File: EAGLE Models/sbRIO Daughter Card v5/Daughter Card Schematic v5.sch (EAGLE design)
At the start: 110 parts, among them Q1 MMBT4403-7-F, Q10 MMBT4403-7-F, Q11 MMBT4401-7-F, Q13 MMBT4401-7-F, Q14 MMBT4403-7-F, Q15 MMBT4403-7-F, Q16 MMBT4403-7-F, Q17 MMBT4403-7-F, Q2 MMBT4403-7-F, Q3 MMBT4403-7-F, Q4 MMBT4403-7-F, Q5 MMBT4403-7-F, Q6 MMBT4403-7-F, Q7 MMBT4403-7-F, Q8 MMBT4403-7-F, Q9 MMBT4401-7-F, U1 MMBT4403-7-F, U2 ADXL345, U3 L3G4200D

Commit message: made many changes
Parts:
- removed DASHBOARD_CONN, HV_BOX_CONN, PEDAL_CONN, SHOCK_POT_CONN, WHEEL_SPEED: EN3_PCB_8, formula electric:EN3_PCB_8
- removed Q14, Q15, Q16, Q17: MMBT4403-7-F, formula electric:MMBT4403-7-F
- removed R26, R28, R30, R32: 10k, resistor:R-US_R0402
- removed R27, R29, R31, R33: 1k, resistor:R-US_R0402
- added ACCUMULATOR_CONN: RJ45-6L21-S, con-tycoelectronics:RJ45-6L21-S
- added AIO_PO_CONN, TUB_CONN: 2516-5, con-3m:2516-5
- added F19, F20, F21, F22, F23, F24, F25, F26: (no value), resistor:R-EU_R0402
- added Q12, Q18, Q19, Q20: MMBT4403-7-F, formula electric:MMBT4403-7-F
- added R37, R38, R39, R40, R41, R42, R43, R44: 4.7k, resistor:R-US_R0402
- added U$1, U$4, U$5, U$6: MMBT4401-7-F, formula electric:MMBT4401-7-F
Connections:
- removed net N$84: Q17.B, R32.2
- new net DIO25: R41.1
- new net DIO26: R37.2
- new net DIO27: R38.2
- new net DIO28: R39.2
- new net N$29: AIO_PO_CONN-3.KL, F19.2
- new net N$30: Q19.B, R40.2
- new net N$31: R40.1, U$1.C
- new net N$32: R41.2, U$1.B
- new net N$85: Q12.B, R42.2
- new net N$86: R42.1, U$4.C
- new net N$87: R37.1, U$4.B
- new net N$88: Q18.B, R43.2
- new net N$89: R43.1, U$5.C
- new net N$90: R38.1, U$5.B
- new net N$91: Q20.B, R44.2
- new net N$92: R44.1, U$6.C
- new net N$93: R39.1, U$6.B
- new net PO1: F26.1, Q19.C
- new net PO2: F25.1, Q12.C
- new net PO3: F24.1, Q18.C
- new net PO4: F23.1, Q20.C
- net 12V: now also F19.1, Q12.E, Q18.E, Q19.E, Q20.E; no longer F15.2
- net 3.3V: no longer Q14.E, Q15.E, Q16.E, Q17.E
- net AI1: now also ACCUMULATOR_CONN.5; no longer HV_BOX_CONN.P$5
- net AI10: now also AIO_PO_CONN-5.KL; no longer SHOCK_POT_CONN.P$2
- net AI11: now also AIO_PO_CONN-4.KL; no longer SHOCK_POT_CONN.P$3
- net AI15: now also AIO_PO_CONN-8.KL
- net AI2: now also ACCUMULATOR_CONN.6; no longer HV_BOX_CONN.P$6
- net AI3: now also TUB_CONN-10.KL; no longer PEDAL_CONN.P$7
- net AI4: now also TUB_CONN-9.KL; no longer PEDAL_CONN.P$8
- net AI7: now also TUB_CONN-13.KL; no longer PEDAL_CONN.P$4
- net AI8: now also AIO_PO_CONN-7.KL; no longer SHOCK_POT_CONN.P$8
- net AI9: now also AIO_PO_CONN-6.KL; no longer SHOCK_POT_CONN.P$1
- net AO0: now also F22.1
- net AO1: now also F21.1
- net AO2: now also F20.1
- net AO3: now also F15.1
- net CAN_GND: now also ACCUMULATOR_CONN.1, ACCUMULATOR_CONN.S@1, ACCUMULATOR_CONN.S@2, ACCUMULATOR_CONN.S@3, ACCUMULATOR_CONN.S@4; no longer HV_BOX_CONN.P$1
- net CAN_H: now also ACCUMULATOR_CONN.3, TUB_CONN-7.KL; no longer DASHBOARD_CONN.P$2, HV_BOX_CONN.P$3
- net CAN_L: now also ACCUMULATOR_CONN.4, TUB_CONN-6.KL; no longer DASHBOARD_CONN.P$3, HV_BOX_CONN.P$4
- net DI09: now also TUB_CONN-8.KL; no longer DASHBOARD_CONN.P$1
- net DIO0: no longer Q14.C, R27.2
- net DIO1: no longer Q17.C, R33.2
- net DIO2: no longer Q16.C, R31.2
- net DIO3: no longer Q15.C, R29.2
- net GND: now also AIO_PO_CONN-1.KL, TUB_CONN-11.KL, U$1.E, U$4.E, U$5.E, U$6.E; no longer R27.1, R29.1, R31.1, R33.1, SHOCK_POT_CONN.P$7, WHEEL_SPEED.P$5
- net N$10: now also AIO_PO_CONN-12.KL, F22.2; no longer R26.1, WHEEL_SPEED.P$8
- net N$13: now also ACCUMULATOR_CONN.7; no longer HV_BOX_CONN.P$7
- net N$14: now also ACCUMULATOR_CONN.8; no longer HV_BOX_CONN.P$8
- net N$20: now also AIO_PO_CONN-2.KL; no longer SHOCK_POT_CONN.P$4
- net N$21: now also AIO_PO_CONN-13.KL, F23.2; no longer F15.1, WHEEL_SPEED.P$4
- net N$22: now also TUB_CONN-12.KL; no longer PEDAL_CONN.P$5
- net N$23: now also TUB_CONN-5.KL; no longer DASHBOARD_CONN.P$4
- net N$24: now also TUB_CONN-4.KL; no longer DASHBOARD_CONN.P$5
- net N$3: now also AIO_PO_CONN-9.KL, F15.2; no longer R32.1, WHEEL_SPEED.P$1
- net N$33: now also TUB_CONN-3.KL; no longer DASHBOARD_CONN.P$6
- net N$34: now also TUB_CONN-2.KL; no longer DASHBOARD_CONN.P$7
- net N$35: now also TUB_CONN-1.KL; no longer DASHBOARD_CONN.P$8
- net N$6: now also AIO_PO_CONN-10.KL, F20.2; no longer Q16.B, R30.2
- net N$81: now also AIO_PO_CONN-14.KL, F24.2; no longer Q14.B, R26.2
- net N$82: now also AIO_PO_CONN-15.KL, F25.2; no longer Q15.B, R28.2
- net N$83: now also AIO_PO_CONN-16.KL, F26.2; no longer R30.1, WHEEL_SPEED.P$2
- net N$9: now also AIO_PO_CONN-11.KL, F21.2; no longer R28.1, WHEEL_SPEED.P$3
- net SHIELD: now also ACCUMULATOR_CONN.2; no longer HV_BOX_CONN.P$2
- net STEERING_POS: now also TUB_CONN-14.KL; no longer PEDAL_CONN.P$3
- net THROTTLE_1: now also TUB_CONN-16.KL; no longer PEDAL_CONN.P$1
- net THROTTLE_2: now also TUB_CONN-15.KL; no longer PEDAL_CONN.P$2
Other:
- note added: "need fusing"
- moved on the sheet: D5, D6, F10, F11, F12, F13, F14, F15, F16, F7, F8, F9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

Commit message: Changed daughter card stuff
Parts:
- removed Q12, Q18, Q19, Q20: MMBT4403-7-F, formula electric:MMBT4403-7-F
- removed R37, R38, R39, R40, R41, R42, R43, R44: 4.7k, resistor:R-US_R0402
- removed U$1, U$4, U$5, U$6: MMBT4401-7-F, formula electric:MMBT4401-7-F
- added IC1: ITS4880R-PAD, infineon:ITS4880R-PAD
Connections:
- removed net DIO25: R41.1
- removed net DIO26: R37.2
- removed net N$30: Q19.B, R40.2
- removed net N$87: R37.1, U$4.B
- removed net N$88: Q18.B, R43.2
- removed net N$89: R43.1, U$5.C
- removed net N$90: R38.1, U$5.B
- removed net N$91: Q20.B, R44.2
- removed net N$92: R44.1, U$6.C
- removed net N$93: R39.1, U$6.B
- net 12V: now also IC1''.LS, IC1''.VBB, IC1''.VBB@1; no longer Q12.E, Q18.E, Q19.E, Q20.E
- net DIO27: now also IC1''.IN3; no longer R38.2
- net DIO28: now also IC1''.IN4; no longer R39.2
- net GND: now also IC1''.GND; no longer U$1.E, U$4.E, U$5.E, U$6.E
- net N$31: now also IC1''.OUT5, IC1''.OUT5@2; no longer R40.1, U$1.C
- net N$32: now also IC1''.OUT6, IC1''.OUT6@2; no longer R41.2, U$1.B
- net N$85: now also IC1''.OUT7, IC1''.OUT7@2; no longer Q12.B, R42.2
- net N$86: now also IC1''.OUT8, IC1''.OUT8@2; no longer R42.1, U$4.C
- net PO1: now also IC1''.OUT1, IC1''.OUT1@2; no longer Q19.C
- net PO2: now also IC1''.OUT2, IC1''.OUT2@2; no longer Q12.C
- net PO3: now also IC1''.OUT3, IC1''.OUT3@2; no longer Q18.C
- net PO4: now also IC1''.OUT4, IC1''.OUT4@2; no longer Q20.C

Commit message: stuff
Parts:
- removed F11, F12, F13, F14, F23, F24, F25, F26: (no value), resistor:R-EU_R0402
- removed Q3, Q4, Q5, Q6: MMBT4403-7-F, formula electric:MMBT4403-7-F
- removed R10, R18, R19, R20, R21, R5, R6, R7: 4.7k, resistor:R-US_R0402
- removed U$17, U$18, U$19, U$20: MMBT4401-7-F, formula electric:MMBT4401-7-F
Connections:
- removed net N$21: AIO_PO_CONN-13.KL, F23.2
- removed net N$24: F11.1, TUB_CONN-4.KL
- removed net N$31: IC1''.OUT5, IC1''.OUT5@2
- removed net N$32: IC1''.OUT6, IC1''.OUT6@2
- removed net N$33: F12.1, TUB_CONN-3.KL
- removed net N$34: F13.1, TUB_CONN-2.KL
- removed net N$35: F14.1, TUB_CONN-1.KL
- removed net N$5: Q6.B, R21.2
- removed net N$50: Q5.B, R5.2
- removed net N$51: Q3.B, R19.2
- removed net N$64: R5.1, U$17.C
- removed net N$65: R18.2, U$17.B
- removed net N$66: R19.1, U$18.C
- removed net N$67: R6.1, U$18.B
- removed net N$68: Q4.B, R20.2
- removed net N$69: R20.1, U$19.C
- removed net N$70: R7.1, U$19.B
- removed net N$71: R21.1, U$20.C
- removed net N$72: R10.1, U$20.B
- removed net N$82: AIO_PO_CONN-15.KL, F25.2
- removed net N$85: IC1''.OUT7, IC1''.OUT7@2
- removed net N$86: IC1''.OUT8, IC1''.OUT8@2
- new net DIO25: IC1''.IN1
- new net DIO26: IC1''.IN2
- net 12V: no longer Q3.E, Q4.E, Q5.E, Q6.E
- net AMS_OUT: now also IC1''.OUT5, IC1''.OUT5@2; no longer F12.2, Q5.C
- net BSPD_OUT: now also IC1''.OUT7, IC1''.OUT7@2; no longer F14.2, Q4.C
- net BUZZER_OUT: now also IC1''.OUT8, IC1''.OUT8@2; no longer F11.2, Q6.C
- net DIO14: now also IC1''.IN8; no longer R10.2
- net DIO6: now also IC1''.IN5; no longer R18.1
- net DIO7: now also IC1''.IN6; no longer R6.2
- net DIO8: now also IC1''.IN7; no longer R7.2
- net GND: no longer U$17.E, U$18.E, U$19.E, U$20.E
- net IMD_OUT: now also IC1''.OUT6, IC1''.OUT6@2; no longer F13.2, Q3.C
- net N$81: no longer F24.2
- net N$83: no longer F26.2
- net PO1: no longer F26.1
- net PO2: no longer F25.1
- net PO3: no longer F24.1
- net PO4: no longer F23.1
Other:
- moved on the sheet: F10, F9, IC1, R36, TUB_CONN-1, TUB_CONN-10, TUB_CONN-11, TUB_CONN-12, TUB_CONN-13, TUB_CONN-14, TUB_CONN-15, TUB_CONN-16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

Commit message: Committed daughter card before autorouting
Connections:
- net N$17 renamed DIO23
- net N$18 renamed DIO24
- removed net N$25: U$3.DIO25
- removed net N$26: U$3.DIO26
- removed net N$27: U$3.DIO27
- removed net N$28: U$3.DIO28
- removed net N$81: AIO_PO_CONN-14.KL
- removed net N$83: AIO_PO_CONN-16.KL
- new net N$21: IC1P1.VBB@9
- new net N$5: IC1P1.VBB@4, IC1P1.VBB@5
- net 12V: now also IC1P1.VBB@10
- net DIO25: now also U$3.DIO25
- net DIO26: now also U$3.DIO26
- net DIO27: now also U$3.DIO27
- net DIO28: now also U$3.DIO28
- net PO1: now also AIO_PO_CONN-16.KL
- net PO2: now also AIO_PO_CONN-15.KL
- net PO3: now also AIO_PO_CONN-14.KL
- net PO4: now also AIO_PO_CONN-13.KL

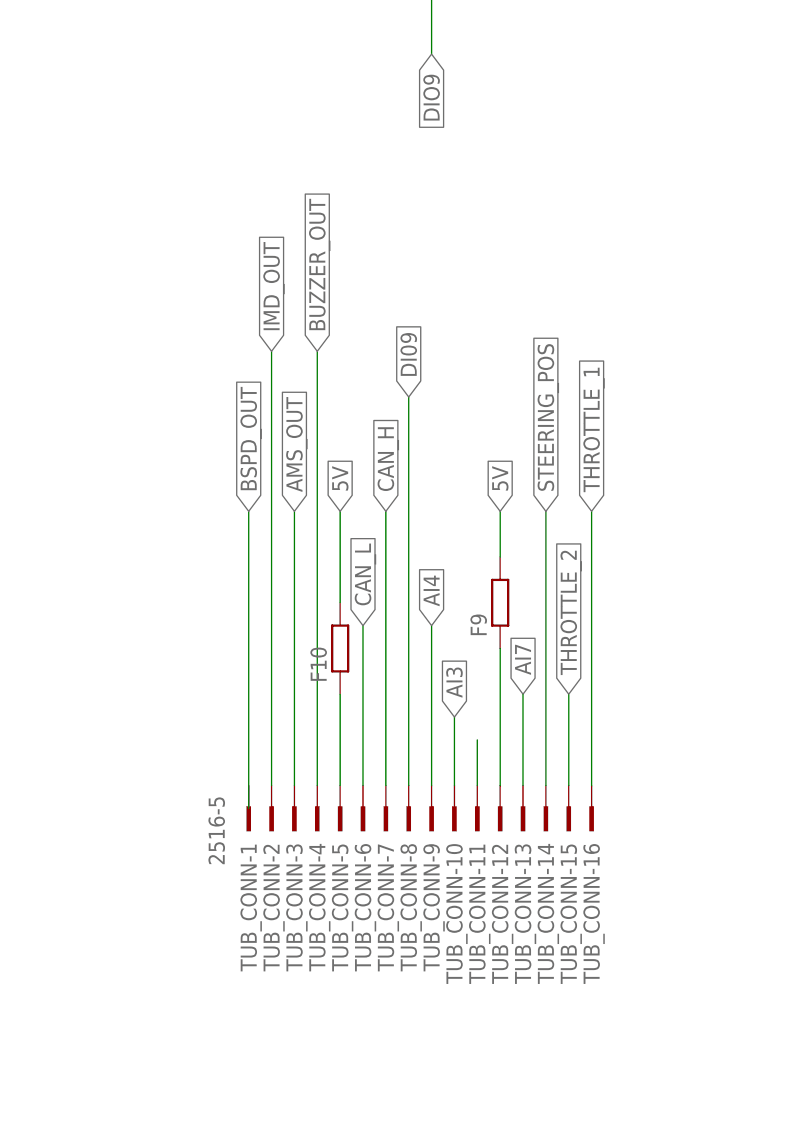
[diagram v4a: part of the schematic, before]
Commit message: fixed four outputs not connected in schematic
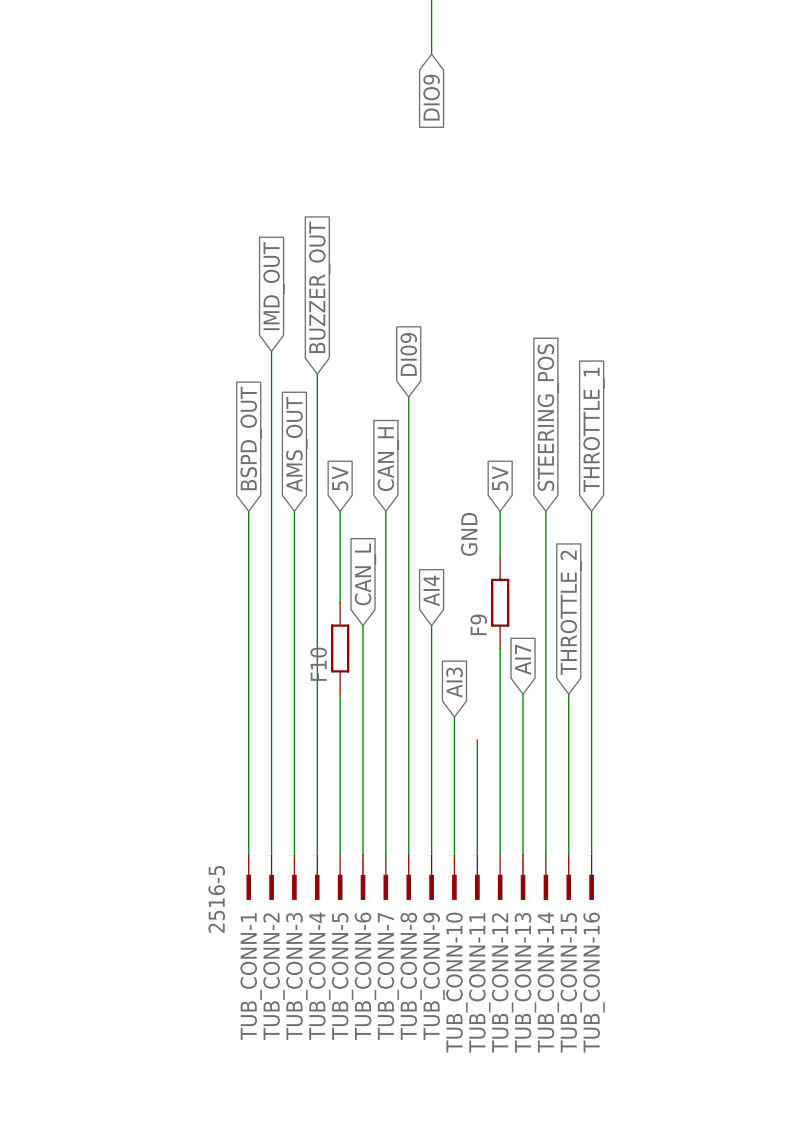
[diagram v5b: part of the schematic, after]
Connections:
- net AMS_OUT: now also TUB_CONN-3.KL
- net BSPD_OUT: now also TUB_CONN-1.KL
- net BUZZER_OUT: now also TUB_CONN-4.KL
- net IMD_OUT: now also TUB_CONN-2.KL
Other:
- moved on the sheet: TUB_CONN-1, TUB_CONN-10, TUB_CONN-11, TUB_CONN-12, TUB_CONN-13, TUB_CONN-14, TUB_CONN-15, TUB_CONN-16, TUB_CONN-2, TUB_CONN-3, TUB_CONN-4, TUB_CONN-5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
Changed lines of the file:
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@@
 <instance part="F21" gate="G$1" x="154.94" y="-162.56" rot="R270"/>
 <instance part="F22" gate="G$1" x="157.48" y="-172.72" rot="R270"/>
-<instance part="TUB_CONN" gate="-1" x="-40.64" y="-180.34" rot="R90"/>
-<instance part="TUB_CONN" gate="-2" x="-38.1" y="-180.34" rot="R90"/>
-<instance part="TUB_CONN" gate="-3" x="-35.56" y="-180.34" rot="R90"/>
-<instance part="TUB_CONN" gate="-4" x="-33.02" y="-180.34" rot="R90"/>
-<instance part="TUB_CONN" gate="-5" x="-30.48" y="-180.34" rot="R90"/>
-<instance part="TUB_CONN" gate="-6" x="-27.94" y="-180.34" rot="R90"/>
-<instance part="TUB_CONN" gate="-7" x="-25.4" y="-180.34" rot="R90"/>
-<instance part="TUB_CONN" gate="-8" x="-22.86" y="-180.34" rot="R90"/>
-<instance part="TUB_CONN" gate="-9" x="-20.32" y="-180.34" rot="R90"/>
-<instance part="TUB_CONN" gate="-10" x="-17.78" y="-180.34" rot="R90"/>
-<instance part="TUB_CONN" gate="-11" x="-15.24" y="-180.34" rot="R90"/>
-<instance part="TUB_CONN" gate="-12" x="-12.7" y="-180.34" rot="R90"/>
-<instance part="TUB_CONN" gate="-13" x="-10.16" y="-180.34" rot="R90"/>
-<instance part="TUB_CONN" gate="-14" x="-7.62" y="-180.34" rot="R90"/>
-<instance part="TUB_CONN" gate="-15" x="-5.08" y="-180.34" rot="R90"/>
-<instance part="TUB_CONN" gate="-16" x="-2.54" y="-180.34" rot="R90"/>
+<instance part="TUB_CONN" gate="-1" x="-40.64" y="-187.96" rot="R90"/>
+<instance part="TUB_CONN" gate="-2" x="-38.1" y="-187.96" rot="R90"/>
+<instance part="TUB_CONN" gate="-3" x="-35.56" y="-187.96" rot="R90"/>
+<instance part="TUB_CONN" gate="-4" x="-33.02" y="-187.96" rot="R90"/>
+<instance part="TUB_CONN" gate="-5" x="-30.48" y="-187.96" rot="R90"/>
+<instance part="TUB_CONN" gate="-6" x="-27.94" y="-187.96" rot="R90"/>
+<instance part="TUB_CONN" gate="-7" x="-25.4" y="-187.96" rot="R90"/>
+<instance part="TUB_CONN" gate="-8" x="-22.86" y="-187.96" rot="R90"/>
+<instance part="TUB_CONN" gate="-9" x="-20.32" y="-187.96" rot="R90"/>
+<instance part="TUB_CONN" gate="-10" x="-17.78" y="-187.96" rot="R90"/>
+<instance part="TUB_CONN" gate="-11" x="-15.24" y="-187.96" rot="R90"/>
+<instance part="TUB_CONN" gate="-12" x="-12.7" y="-187.96" rot="R90"/>
+<instance part="TUB_CONN" gate="-13" x="-10.16" y="-187.96" rot="R90"/>
+<instance part="TUB_CONN" gate="-14" x="-7.62" y="-187.96" rot="R90"/>
+<instance part="TUB_CONN" gate="-15" x="-5.08" y="-187.96" rot="R90"/>
+<instance part="TUB_CONN" gate="-16" x="-2.54" y="-187.96" rot="R90"/>
 <instance part="IC1" gate="''" x="149.86" y="-68.58" rot="R270"/>
 <instance part="IC1" gate="P1" x="215.9" y="-50.8"/>
@@
 </segment>
 <segment>
-<wire x1="-15.24" y1="-170.18" x2="-15.24" y2="-175.26" width="0.1524" layer="91"/>
+<wire x1="-15.24" y1="-170.18" x2="-15.24" y2="-182.88" width="0.1524" layer="91"/>
 <pinref part="TUB_CONN" gate="-11" pin="KL"/>
+<label x="-15.24" y="-149.86" size="1.778" layer="95" rot="R90"/>
 </segment>
 <segment>
@@
 </segment>
 <segment>
-<wire x1="-25.4" y1="-144.78" x2="-25.4" y2="-175.26" width="0.1524" layer="91"/>
+<wire x1="-25.4" y1="-144.78" x2="-25.4" y2="-182.88" width="0.1524" layer="91"/>
 <label x="-25.4" y="-144.78" size="1.778" layer="95" rot="R90" xref="yes"/>
 <pinref part="TUB_CONN" gate="-7" pin="KL"/>
@@
 </segment>
 <segment>
-<wire x1="-27.94" y1="-157.48" x2="-27.94" y2="-175.26" width="0.1524" layer="91"/>
+<wire x1="-27.94" y1="-157.48" x2="-27.94" y2="-182.88" width="0.1524" layer="91"/>
 <label x="-27.94" y="-157.48" size="1.778" layer="95" rot="R90" xref="yes"/>
 <pinref part="TUB_CONN" gate="-6" pin="KL"/>
@@
 </segment>
 <segment>
-<wire x1="-17.78" y1="-175.26" x2="-17.78" y2="-167.64" width="0.1524" layer="91"/>
+<wire x1="-17.78" y1="-182.88" x2="-17.78" y2="-167.64" width="0.1524" layer="91"/>
 <label x="-17.78" y="-167.64" size="1.778" layer="95" rot="R90" xref="yes"/>
 <pinref part="TUB_CONN" gate="-10" pin="KL"/>
@@
 </segment>
 <segment>
-<wire x1="-20.32" y1="-175.26" x2="-20.32" y2="-157.48" width="0.1524" layer="91"/>
+<wire x1="-20.32" y1="-182.88" x2="-20.32" y2="-157.48" width="0.1524" layer="91"/>
 <label x="-20.32" y="-157.48" size="1.778" layer="95" rot="R90" xref="yes"/>
 <pinref part="TUB_CONN" gate="-9" pin="KL"/>
@@
 </segment>
 <segment>
-<wire x1="-2.54" y1="-175.26" x2="-2.54" y2="-144.78" width="0.1524" layer="91"/>
+<wire x1="-2.54" y1="-182.88" x2="-2.54" y2="-144.78" width="0.1524" layer="91"/>
 <label x="-2.54" y="-144.78" size="1.778" layer="95" rot="R90" xref="yes"/>
 <pinref part="TUB_CONN" gate="-16" pin="KL"/>
@@
 </segment>
 <segment>
-<wire x1="-5.08" y1="-175.26" x2="-5.08" y2="-165.1" width="0.1524" layer="91"/>
+<wire x1="-5.08" y1="-182.88" x2="-5.08" y2="-165.1" width="0.1524" layer="91"/>
 <label x="-5.08" y="-165.1" size="1.778" layer="95" rot="R90" xref="yes"/>
 <pinref part="TUB_CONN" gate="-15" pin="KL"/>
@@
 </segment>
 <segment>
-<wire x1="-10.16" y1="-175.26" x2="-10.16" y2="-165.1" width="0.1524" layer="91"/>
+<wire x1="-10.16" y1="-182.88" x2="-10.16" y2="-165.1" width="0.1524" layer="91"/>
 <label x="-10.16" y="-165.1" size="1.778" layer="95" rot="R90" xref="yes"/>
 <pinref part="TUB_CONN" gate="-13" pin="KL"/>
@@
 <net name="AMS_OUT" class="0">
 <segment>
-<wire x1="-35.56" y1="-175.26" x2="-35.56" y2="-144.78" width="0.1524" layer="91"/>
+<wire x1="-35.56" y1="-182.88" x2="-35.56" y2="-144.78" width="0.1524" layer="91"/>
 <label x="-35.56" y="-144.78" size="1.778" layer="95" rot="R90" xref="yes"/>
+<pinref part="TUB_CONN" gate="-3" pin="KL"/>
 </segment>
 <segment>
@@
 <net name="IMD_OUT" class="0">
 <segment>
-<wire x1="-38.1" y1="-175.26" x2="-38.1" y2="-127" width="0.1524" layer="91"/>
+<wire x1="-38.1" y1="-182.88" x2="-38.1" y2="-127" width="0.1524" layer="91"/>
 <label x="-38.1" y="-127" size="1.778" layer="95" rot="R90" xref="yes"/>
+<pinref part="TUB_CONN" gate="-2" pin="KL"/>
 </segment>
 <segment>
@@
 <net name="BSPD_OUT" class="0">
 <segment>
-<wire x1="-40.64" y1="-177.8" x2="-40.64" y2="-144.78" width="0.1524" layer="91"/>
+<wire x1="-40.64" y1="-182.88" x2="-40.64" y2="-144.78" width="0.1524" layer="91"/>
 <label x="-40.64" y="-144.78" size="1.778" layer="95" rot="R90" xref="yes"/>
+<pinref part="TUB_CONN" gate="-1" pin="KL"/>
 </segment>
 <segment>
@@
 </segment>
 <segment>
-<wire x1="-7.62" y1="-175.26" x2="-7.62" y2="-144.78" width="0.1524" layer="91"/>
+<wire x1="-7.62" y1="-182.88" x2="-7.62" y2="-144.78" width="0.1524" layer="91"/>
 <label x="-7.62" y="-144.78" size="1.778" layer="95" rot="R90" xref="yes"/>
 <pinref part="TUB_CONN" gate="-14" pin="KL"/>
@@
 <net name="BUZZER_OUT" class="0">
 <segment>
-<wire x1="-33.02" y1="-175.26" x2="-33.02" y2="-127" width="0.1524" layer="91"/>
-<label x="-33.02" y="-127" size="1.778" layer="95" rot="R90" xref="yes"/>
+<wire x1="-33.02" y1="-182.88" x2="-33.02" y2="-129.54" width="0.1524" layer="91"/>
+<label x="-33.02" y="-129.54" size="1.778" layer="95" rot="R90" xref="yes"/>
+<pinref part="TUB_CONN" gate="-4" pin="KL"/>
 </segment>
 <segment>
@@
 <net name="DI09" class="0">
 <segment>
-<wire x1="-22.86" y1="-175.26" x2="-22.86" y2="-132.08" width="0.1524" layer="91"/>
+<wire x1="-22.86" y1="-182.88" x2="-22.86" y2="-132.08" width="0.1524" layer="91"/>
 <label x="-22.86" y="-132.08" size="1.778" layer="95" rot="R90" xref="yes"/>
 <pinref part="TUB_CONN" gate="-8" pin="KL"/>
@@
 <segment>
 <pinref part="F9" gate="G$1" pin="1"/>
-<wire x1="-12.7" y1="-175.26" x2="-12.7" y2="-160.02" width="0.1524" layer="91"/>
+<wire x1="-12.7" y1="-182.88" x2="-12.7" y2="-160.02" width="0.1524" layer="91"/>
 <pinref part="TUB_CONN" gate="-12" pin="KL"/>
 </segment>
@@
 <segment>
 <pinref part="F10" gate="G$1" pin="1"/>
-<wire x1="-30.48" y1="-165.1" x2="-30.48" y2="-175.26" width="0.1524" layer="91"/>
+<wire x1="-30.48" y1="-165.1" x2="-30.48" y2="-182.88" width="0.1524" layer="91"/>
 <pinref part="TUB_CONN" gate="-5" pin="KL"/>
 </segment>

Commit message: did more things
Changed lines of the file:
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@@
 <wire x1="-15.24" y1="-170.18" x2="-15.24" y2="-182.88" width="0.1524" layer="91"/>
 <pinref part="TUB_CONN" gate="-11" pin="KL"/>
-<label x="-15.24" y="-149.86" size="1.778" layer="95" rot="R90"/>
 </segment>
 <segment>
@@
 <net name="BUZZER_OUT" class="0">
 <segment>
-<wire x1="-33.02" y1="-182.88" x2="-33.02" y2="-129.54" width="0.1524" layer="91"/>
-<label x="-33.02" y="-129.54" size="1.778" layer="95" rot="R90" xref="yes"/>
+<wire x1="-33.02" y1="-182.88" x2="-33.02" y2="-127" width="0.1524" layer="91"/>
+<label x="-33.02" y="-127" size="1.778" layer="95" rot="R90" xref="yes"/>
 <pinref part="TUB_CONN" gate="-4" pin="KL"/>
 </segment>
